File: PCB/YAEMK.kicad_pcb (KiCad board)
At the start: 2 copper layers, 165.8 x 130.8 mm, 222 parts, among them J1 DBG, P1 PC, P2 Link, P3 SSD1107, Q1 MMUN2133LT1G, Q2 DMMT5401, Q3 AO3401A, SW1 ALPS EC11, U1 24LC64, U2 SSP6206, U3 USBLC6-2SC6, U4 USBLC6-2SC6, U5 STM32F303CCTx

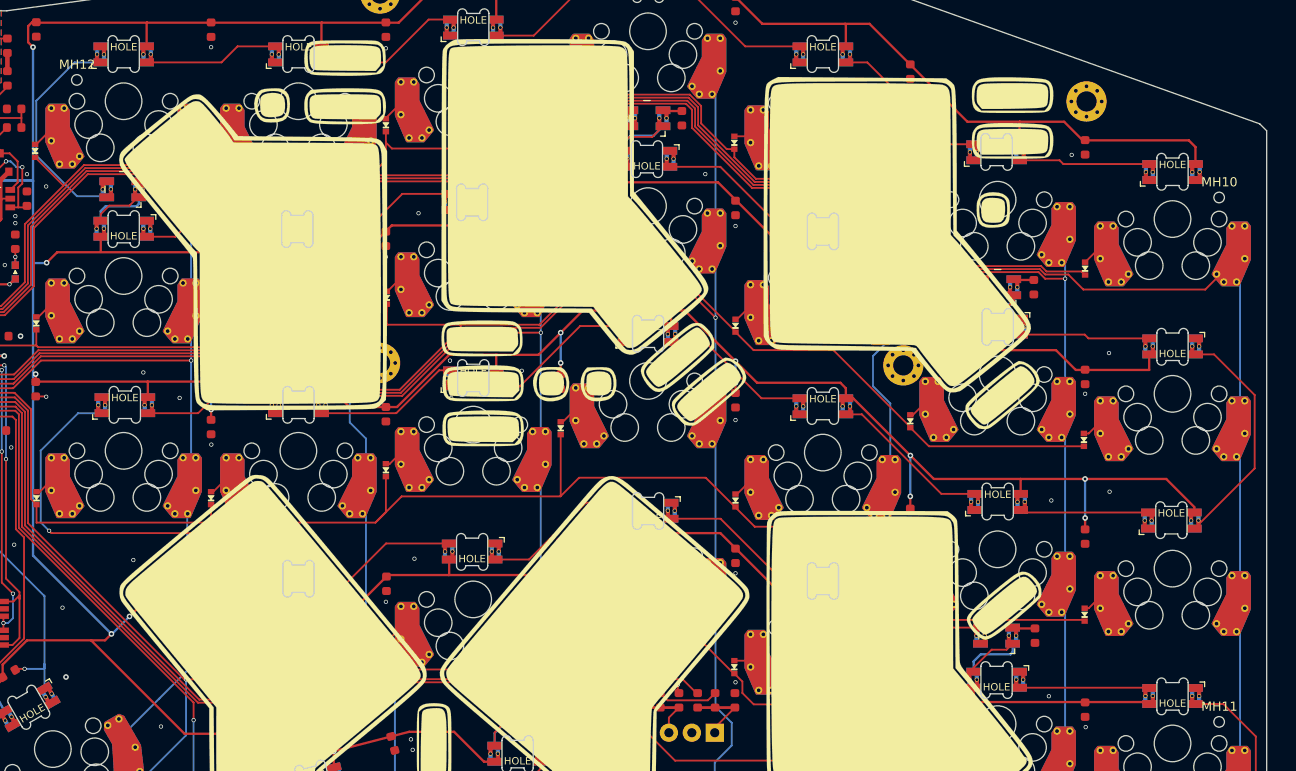
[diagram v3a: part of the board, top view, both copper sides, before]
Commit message: Add logos as symbols, clean up symbols
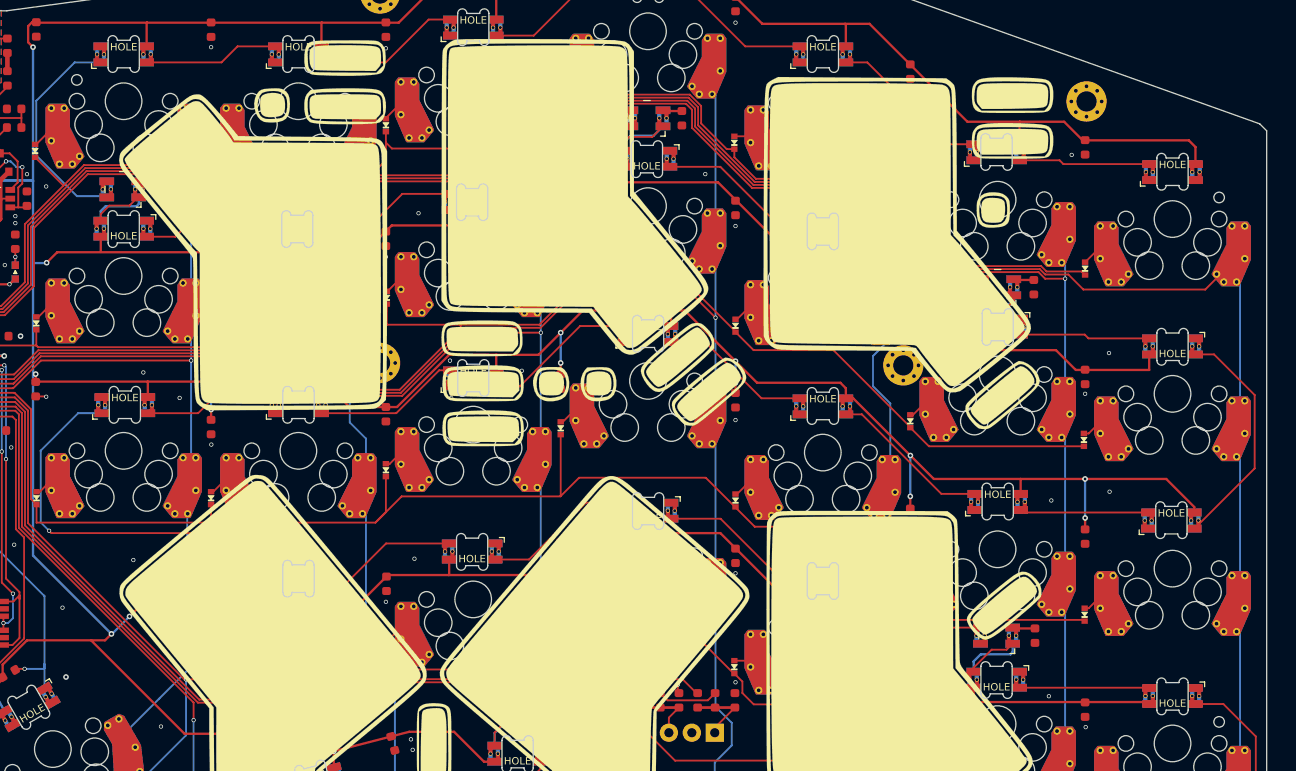
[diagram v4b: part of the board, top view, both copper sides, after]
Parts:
- G1, G2: renamed from G***; value LOGO -> Logo
- MH10, MH11, MH12: value MOUNT_HOLE -> Assembly Hole
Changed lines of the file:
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@@
     (0 Front signal)
     (31 Back signal)
-    (36 B.SilkS user hide)
+    (36 B.SilkS user)
     (37 F.SilkS user hide)
     (38 B.Mask user)
@@
   (module prettylib:JLC_SMT_Assembly_Hole (layer Front)
     (at 101.6 40.894)
-    (fp_text reference MH12 (at 0 0.5) (layer F.SilkS)
+    (fp_text reference MH12 (at 0 0.5) (layer F.SilkS) hide
       (effects (font (size 1 1) (thickness 0.15)))
     )
-    (fp_text value MOUNT_HOLE (at 0 -0.5) (layer F.Fab)
+    (fp_text value "Assembly Hole" (at 0 -0.5) (layer F.Fab) hide
       (effects (font (size 1 1) (thickness 0.15)))
     )
@@
   (module prettylib:JLC_SMT_Assembly_Hole (layer Front)
     (at 226.085 110.855)
-    (fp_text reference MH11 (at 0 0.5) (layer F.SilkS)
+    (fp_text reference MH11 (at 0 0.5) (layer F.SilkS) hide
       (effects (font (size 1 1) (thickness 0.15)))
     )
-    (fp_text value MOUNT_HOLE (at 0 -0.5) (layer F.Fab)
+    (fp_text value "Assembly Hole" (at 0 -0.5) (layer F.Fab) hide
       (effects (font (size 1 1) (thickness 0.15)))
     )
@@
   (module prettylib:JLC_SMT_Assembly_Hole (layer Front)
     (at 226.085 53.705)
-    (fp_text reference MH10 (at 0 0.5) (layer F.SilkS)
+    (fp_text reference MH10 (at 0 0.5) (layer F.SilkS) hide
       (effects (font (size 1 1) (thickness 0.15)))
     )
-    (fp_text value MOUNT_HOLE (at 0 -0.5) (layer F.Fab)
+    (fp_text value "Assembly Hole" (at 0 -0.5) (layer F.Fab) hide
       (effects (font (size 1 1) (thickness 0.15)))
     )
@@
     (at 157.3022 84.455 180)
     (attr smd)
-    (fp_text reference G*** (at 0 0) (layer B.SilkS) hide
+    (fp_text reference G2 (at 0 0) (layer B.SilkS) hide
       (effects (font (size 1.524 1.524) (thickness 0.3)) (justify mirror))
     )
-    (fp_text value LOGO (at 0.75 0) (layer B.SilkS) hide
+    (fp_text value Logo (at 0.75 0) (layer B.SilkS) hide
       (effects (font (size 1.524 1.524) (thickness 0.3)) (justify mirror))
     )
@@
     (at 157.3022 84.5185)
     (attr smd)
-    (fp_text reference G*** (at 0 0) (layer F.SilkS) hide
+    (fp_text reference G1 (at 0 0) (layer F.SilkS) hide
       (effects (font (size 1.524 1.524) (thickness 0.3)))
     )
-    (fp_text value LOGO (at 0.75 0) (layer F.SilkS) hide
+    (fp_text value Logo (at 0.75 0) (layer F.SilkS) hide
       (effects (font (size 1.524 1.524) (thickness 0.3)))
     )
